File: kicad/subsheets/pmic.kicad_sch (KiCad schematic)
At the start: 51 parts, among them U3 RK809-5

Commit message: Annotations + minor tweaks
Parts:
- U3: DATASHEET https://atta.szlcsc.com/upload/public/pdf/source/20240126/F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 -> (none)
- renumbered C39 to C32, C40 to C33, C35 to C34, C36 to C35, C37 to C36, C38 to C37, C41 to C38, C42 to C39, C43 to C40, R38 to R19, R22 to R20, R23 to R21, R24 to R22, R25 to R23, R26 to R24, R19 to R25
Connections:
- net VBUCK5_2V2: now also C31.2, L7.2, U3.59 (FB5); no longer L7.1, U3.53 (SW5)
- net VBUCK1 renamed BUCK1_0V9
- net VBUCK2 renamed BUCK2_0V9
- net VBUCK3 renamed BUCK3_1V35
- net VBUCK4 renamed BUCK4_1V8
- net VLDO1 renamed LDO1_0V9
- net VLDO2 renamed LDO2_0V9
- net VLDO3 renamed LDO3_0V9
- net VLDO4 renamed LDO4_3V3
- net VLDO5 renamed LDO5_3V3
- net VLDO6 renamed LDO6_3V3
- net VLDO7 renamed LDO7_1V8
- net VLDO8 renamed LDO8_1V8
- net VLDO9 renamed LDO9_1V8
- net VSWOUT1 renamed SW1_3V3
- net VSWOUT2 renamed SW2_3V3
- new net: L7.1, U3.53 (SW5)

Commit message: Annotations + minor tweaks
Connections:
- net VBUCK5_2V2 renamed BUCK5_2V2
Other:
- note added: "BUCK5 is otherwise unused. VCC5/7 power LDOs @ 0V9/1V8 so powering them @ 2V2 increases efficiency (needs 400mV margin)"
- note removed: "BUCK5 is otherwise unused VCC5/6 power LDOs @ 0V9/1V8 so powering them @ 2V2 increases efficiency"
- note removed: "CL = (C^2)/(2C) + Cstray = 12.5 pF ? C = 22 pF"

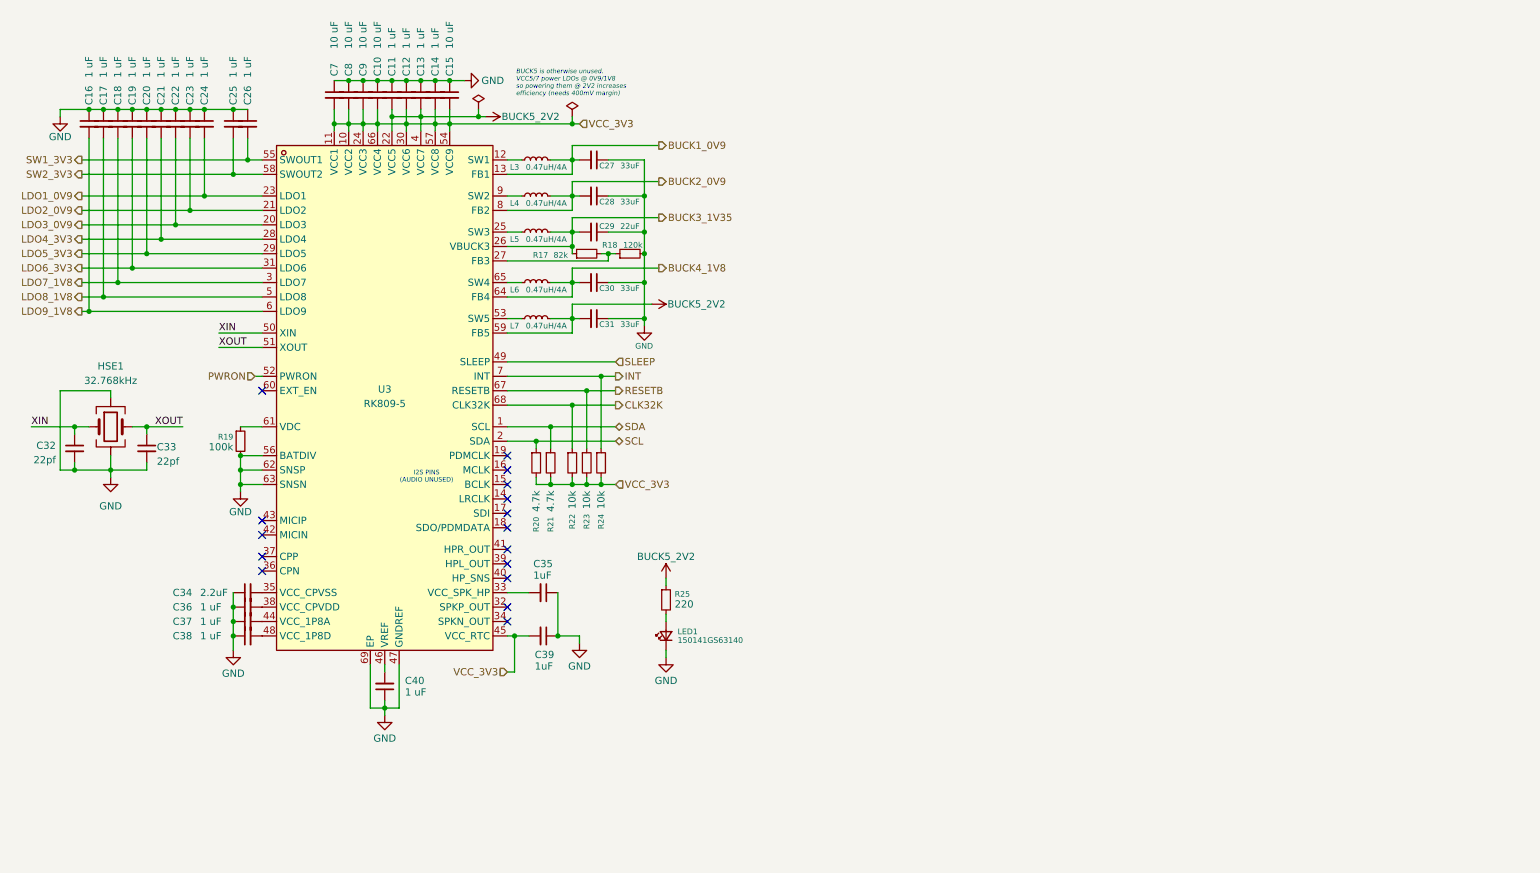
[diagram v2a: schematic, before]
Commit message: Change all sheets to A4, name sheets, split RK3566 into hierarchy
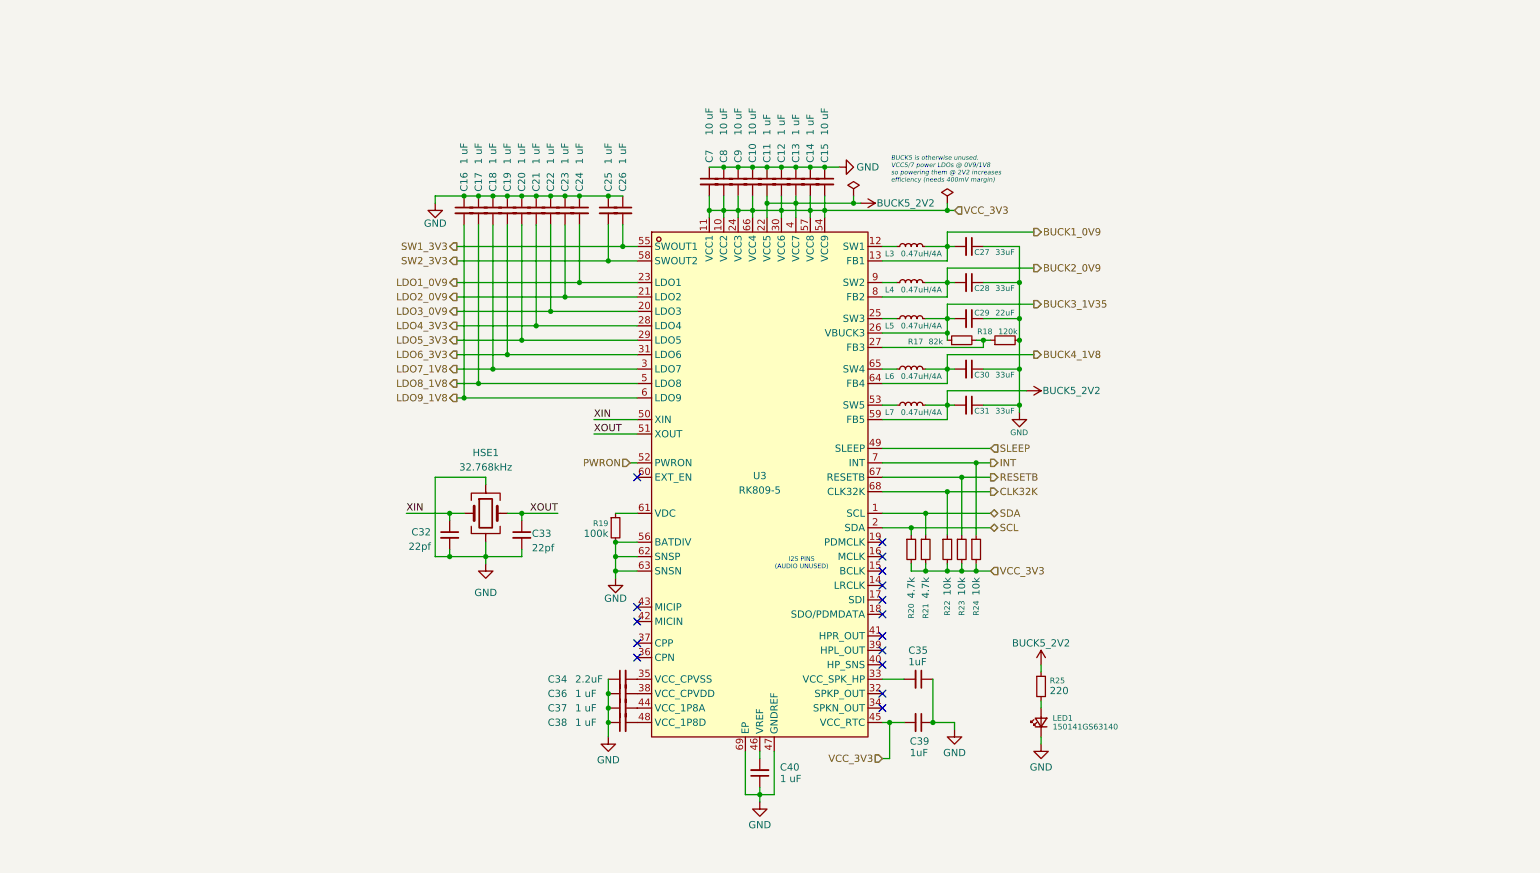
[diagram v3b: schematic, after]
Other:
- title: (none) -> Power Management IC
- moved on the sheet: C10, C11, C12, C13, C14, C15, C16, C17, C18, C19, C20, C21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

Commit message: Mark as R1.0
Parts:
- renumbered C9 to C10, C10 to C11, C11 to C12, C12 to C13, C13 to C14, C14 to C15, C15 to C16, C16 to C17, C17 to C18, C18 to C19, C19 to C20, C20 to C21, C21 to C22, C22 to C23, C23 to C24, C24 to C25, C25 to C26, C26 to C27, C27 to C28, C28 to C29, C29 to C30, C30 to C31, C31 to C32, C32 to C33, C33 to C34, C34 to C35, C35 to C36, C36 to C37, C37 to C38, C38 to C39, C39 to C40, C40 to C41, C7 to C8, C8 to C9, R17 to R19, R18 to R20, R19 to R21, R20 to R22, R21 to R23, R22 to R24, R23 to R25, R24 to R26, R25 to R27
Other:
- company: (none) -> UVic Rocketry

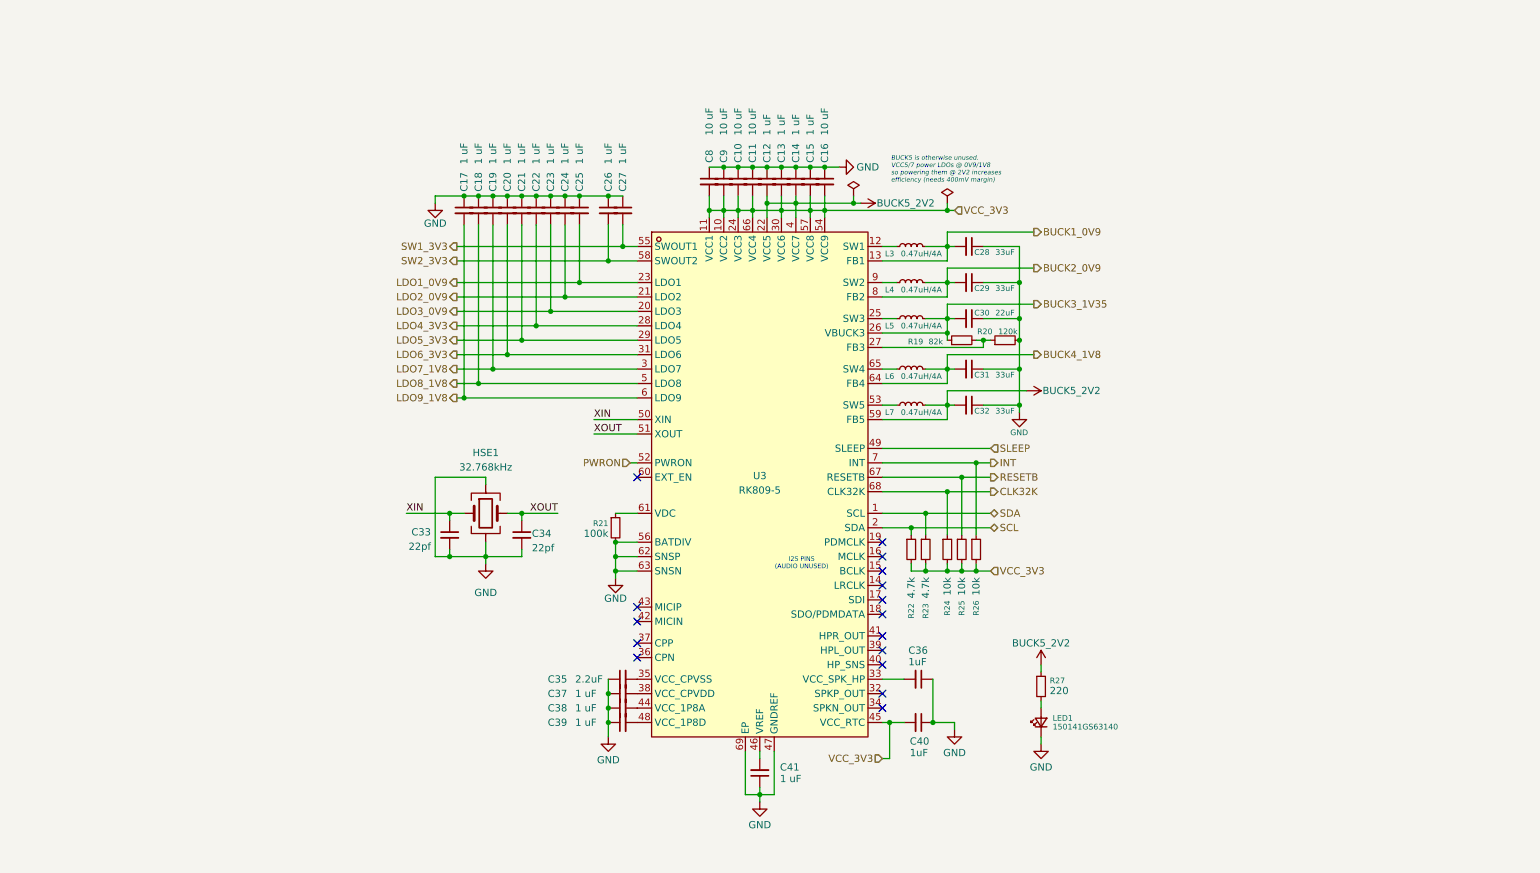
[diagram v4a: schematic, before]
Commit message: Indicate proper feedback trace from SoC
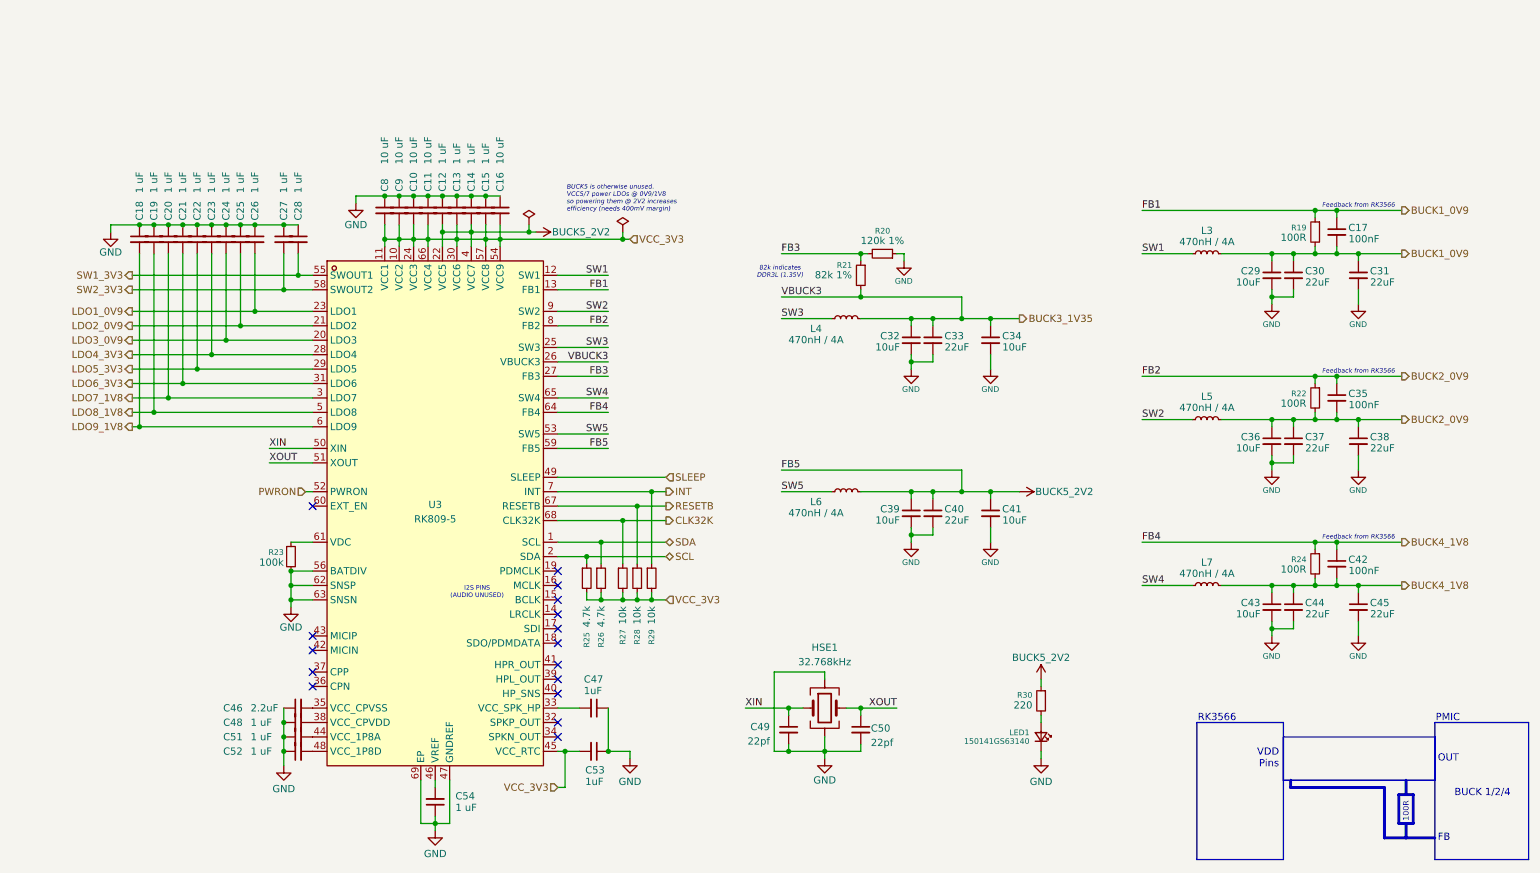
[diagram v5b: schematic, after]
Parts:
- removed C28: 33uF, symbol Device:C_Small
- added C17, C35, C42: 100nF, symbol Device:C_Small
- added C33, C37, C38, C40, C44, C45: 22uF, symbol Device:C_Small
- added C34, C36, C39, C41, C43: 10uF, symbol Device:C_Small
- added R21: 82k 1%, symbol Device:R_Small
- added R22, R24: 100R, symbol Device:R_Small
- C29, C32: value 33uF -> 10uF
- C31: value 33uF -> 22uF
- L3, L4, L5, L6, L7: value 0.47uH/4A -> 470nH / 4A
- R19: value 82k -> 100R
- R20: value 120k -> 120k 1%
- renumbered C17 to C18, C18 to C19, C19 to C20, C20 to C21, C21 to C22, C22 to C23, C23 to C24, C24 to C25, C25 to C26, C26 to C27, C27 to C28, C35 to C46, C36 to C47, C37 to C48, C33 to C49, C34 to C50, C38 to C51, C39 to C52, C40 to C53, C41 to C54, R21 to R23, R22 to R25, R23 to R26, R24 to R27, R25 to R28, R26 to R29, R27 to R30
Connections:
- net BUCK1_0V9: now also C29.1, C30.1, C31.1, R19.1, R19.2, C17.1, C17.2
- net BUCK2_0V9: now also L5.2, C35.1, C35.2, C36.1, C37.1, C38.1, R22.1, R22.2; no longer C29.2, L4.2
- net BUCK3_1V35: now also C32.1, L4.2, C33.1, C34.1, R21.2; no longer C30.2, L5.2, R19.1
- net BUCK4_1V8: now also L7.2, C42.1, C42.2, C43.1, C44.1, C45.1, R24.1, R24.2; no longer C31.2, L6.2
- net BUCK5_2V2: now also L6.2, C39.1, C40.1, C41.1; no longer C32.2, L7.2
- net GND: now also C29.2, C30.2, C31.2, C32.2, R20.1, C33.2, C34.2, C36.2, C37.2, C38.2, C39.2, C40.2, C41.2, C43.2, C44.2, C45.2; no longer C29.1, C30.1, C31.1, C32.1, R20.2
- net SW1: now reaches L3.1, U3.12 (SW1)
- net SW2: now reaches L5.1
- net SW2: now also U3.9 (SW2); no longer U3.25 (SW3)
- net SW4: now reaches L7.1
- net SW4: now also U3.65 (SW4); no longer U3.53 (SW5)
- net SW5: now reaches L6.1
- net SW5: now also U3.53 (SW5); no longer U3.65 (SW4)
- net SW3: now reaches L4.1
- net SW3: now also U3.25 (SW3); no longer U3.9 (SW2)
- new net FB3: R20.2, R21.1, U3.27 (FB3)
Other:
- note added: "100R"
- note added: "82k indicates DDR3L (1.35V)"
- note added: "BUCK 1/2/4"
- note added: "FB"
- note added: "Feedback from RK3566"
- note added: "OUT"
- note added: "PMIC"
- note added: "RK3566"
- note added: "VDD Pins"
- moved on the sheet: C10, C11, C12, C13, C14, C15, C16, C18, C19, C20, C21, C22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

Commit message: Start on PCB design
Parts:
- removed C42: 100nF, symbol Device:C_Small
- removed C43: 10uF, symbol Device:C_Small
- removed C49, C50: 22pf, symbol Device:C_Small
- removed HSE1: 32.768kHz, symbol Device:Crystal_GND24
- removed R24: 100R, symbol Device:R_Small
- added C47, C48: 22pf, Capacitor_SMD:C_0402_1005Metric, symbol Device:C_Small
- added HSE1: 32.768kHz, Crystal:Crystal_SMD_3215-2Pin_3.2x1.5mm, symbol Device:Crystal
- added NT1, NT2, NT3: NetTie_2, symbol Device:NetTie_2
- C10, C11, C16, C8, C9: value 10 uF -> 10uF; footprint (none) -> Capacitor_SMD:C_0805_2012Metric; LCSC PART NAME (none) -> C15850
- C12, C13, C14, C15, C18, C19, C20, C21, C22, C23, C24, C25, C26, C27, C28: value 1 uF -> 1uF; footprint (none) -> Capacitor_SMD:C_0603_1608Metric; LCSC PART NAME (none) -> C15849
- C17, C35: footprint (none) -> Capacitor_SMD:C_0402_1005Metric; LCSC PART NAME (none) -> C1525
- C29, C32, C34, C36, C39, C41: footprint (none) -> Capacitor_SMD:C_0805_2012Metric; LCSC PART NAME (none) -> C15850
- C30, C31, C33, C37, C38, C40: footprint (none) -> Capacitor_SMD:C_1206_3216Metric; LCSC PART NAME (none) -> C12891
- C42: renamed from C45; footprint (none) -> Capacitor_SMD:C_1206_3216Metric; LCSC PART NAME (none) -> C12891
- C43: renamed from C44; footprint (none) -> Capacitor_SMD:C_1206_3216Metric; LCSC PART NAME (none) -> C12891
- C44: renamed from C46; value 2.2uF -> 1uF; footprint (none) -> Capacitor_SMD:C_0603_1608Metric; LCSC PART NAME (none) -> C15849
- C45: renamed from C47; footprint (none) -> Capacitor_SMD:C_0603_1608Metric; LCSC PART NAME (none) -> C15849
- C46: renamed from C48; value 1 uF -> 1uF; footprint (none) -> Capacitor_SMD:C_0603_1608Metric; LCSC PART NAME (none) -> C15849
- C49: renamed from C51; value 1 uF -> 1uF; footprint (none) -> Capacitor_SMD:C_0603_1608Metric; LCSC PART NAME (none) -> C15849
- C50: renamed from C52; value 1 uF -> 1uF; footprint (none) -> Capacitor_SMD:C_0603_1608Metric; LCSC PART NAME (none) -> C15849
- C51: renamed from C53; footprint (none) -> Capacitor_SMD:C_0603_1608Metric; LCSC PART NAME (none) -> C15849
- C52: renamed from C54; value 1 uF -> 1uF; footprint (none) -> Capacitor_SMD:C_0603_1608Metric; LCSC PART NAME (none) -> C15849
- L3, L4, L5, L6, L7: footprint (none) -> Inductor_SMD:L_0805_2012Metric; LCSC PART NAME (none) -> C89446
- LED1: footprint (none) -> LED_SMD:LED_0805_2012Metric; LCSC PART NAME (none) -> C2297
- R21: renamed from R19; footprint (none) -> Resistor_SMD:R_0402_1005Metric; LCSC PART NAME (none) -> C25076
- R22: renamed from R20; value 120k 1% -> 120k; footprint (none) -> Resistor_SMD:R_0603_1608Metric; LCSC PART NAME (none) -> C25808
- R23: renamed from R21; value 82k 1% -> 82k; footprint (none) -> Resistor_SMD:R_0603_1608Metric; LCSC PART NAME (none) -> C23254
- R24: renamed from R22; footprint (none) -> Resistor_SMD:R_0402_1005Metric; LCSC PART NAME (none) -> C25076
- R25: renamed from R23; value 100k -> 10k; footprint (none) -> Resistor_SMD:R_0402_1005Metric; LCSC PART NAME (none) -> C25744
- R26: renamed from R25; footprint (none) -> Resistor_SMD:R_0402_1005Metric; LCSC PART NAME (none) -> C25900
- R27: renamed from R26; footprint (none) -> Resistor_SMD:R_0402_1005Metric; LCSC PART NAME (none) -> C25900
- R28: renamed from R27; footprint (none) -> Resistor_SMD:R_0402_1005Metric; LCSC PART NAME (none) -> C25744
- R29: renamed from R28; footprint (none) -> Resistor_SMD:R_0402_1005Metric; LCSC PART NAME (none) -> C25744
- R30: renamed from R29; footprint (none) -> Resistor_SMD:R_0402_1005Metric; LCSC PART NAME (none) -> C25744
- R31: renamed from R30; value 220 -> 220R; footprint (none) -> Resistor_SMD:R_0603_1608Metric; LCSC PART NAME (none) -> C22962
- U3: LCSC PART NAME RK809-5 -> (none)
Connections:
- net BUCK1_0V9: no longer C17.1, R21.1, U3.13 (FB1)
- net BUCK2_0V9: no longer C35.1, R24.1, U3.8 (FB2)
- net BUCK3_1V35: now also NT1.2; no longer C32.1, C33.1, C34.1, L4.2, R23.2, U3.26 (VBUCK3)
- net BUCK4_1V8: now also NT3.2; no longer C42.1, C43.1, L7.2, U3.64 (FB4)
- net BUCK5_2V2: now also NT2.2; no longer C39.1, C40.1, C41.1, L6.2, U3.59 (FB5)
- net GND: now also C47.2, C48.2
- net XIN: now also C47.1, HSE1.1
- net XOUT: now also C48.1, HSE1.2
- new net FB1: C17.1, R21.1, U3.13 (FB1)
- new net FB2: C35.1, R24.1, U3.8 (FB2)
- new net FB4: C42.1, C43.1, L7.2, NT3.1, U3.64 (FB4)
- new net FB5: C39.1, C40.1, C41.1, L6.2, NT2.1, U3.59 (FB5)
- new net VBUCK3: C32.1, C33.1, C34.1, L4.2, NT1.1, R23.2, U3.26 (VBUCK3)
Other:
- note added: "BUCK 1/2"
- note removed: "BUCK 1/2/4"
- moved on the sheet: C10, C11, C12, C13, C14, C15, C16, C17, C18, C19, C20, C21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

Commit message: Minor tweaks
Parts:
- removed NT2, NT3: NetTie_2, symbol Device:NetTie_2
- added NT4: NetTie_2, symbol Device:NetTie_2
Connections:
- net FB4 is gone; now on net BUCK4_1V8: C42.1, C43.1, L7.2, U3.64 (FB4)
- net FB5 is gone; now on net BUCK5_2V2: C39.1, C40.1, C41.1, L6.2, U3.59 (FB5)
- net VCC_3V3: now also NT4.1; no longer C51.2, U3.45 (VCC_RTC)
- new net VCC_RTC: C51.2, NT4.2, U3.45 (VCC_RTC)
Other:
- moved on the sheet: C41, C51
